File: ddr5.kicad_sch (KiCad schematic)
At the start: 39 parts, among them U1 MT60B2G8HB-48B_A

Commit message: Globlib
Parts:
- C1, C10, C11, C12, C13, C14, C15, C18, C2, C23, C24, C25, C26, C28, C3, C30, C32, C4, C5, C6, C7, C8, C9: footprint ddr5-testbed-footprints:C_0201 -> antmicro-footprints:C_0201; symbol ddr5-testbed:C_100n_0201 -> antmicroCapacitorsmisc:C_100n_0201
- FB1, FB2, FB3: footprint ddr5-testbed-footprints:FB_0805_2012Metric -> antmicro-footprints:FB_0805_2012Metric; symbol ddr5-testbed:FB_220Z_1.5A_0805 -> antmicroFerriteBeadsandChips:FB_220Z_1.5A_WE-CBF_0805
- R1, R5: footprint ddr5-testbed-footprints:R_0402_1005Metric -> antmicro-footprints:R_0402_1005Metric; symbol ddr5-testbed:R_1k_0402 -> antmicroResistors0402:R_1k_0402
- R15, R16, R17, R18, R19, R2, R4, R7: footprint ddr5-testbed-footprints:R_0402_1005Metric -> antmicro-footprints:R_0402_1005Metric; symbol ddr5-testbed:R_0R_0402 -> antmicroResistors0402:R_0R_0402
- R3: footprint ddr5-testbed-footprints:R_0402_1005Metric -> antmicro-footprints:R_0402_1005Metric; symbol ddr5-testbed:R_10k_0402 -> antmicroResistors0402:R_10k_0402
- R6: footprint ddr5-testbed-footprints:R_0402_1005Metric -> antmicro-footprints:R_0402_1005Metric; symbol ddr5-testbed:R_240R_0402 -> antmicroResistors0402:R_240R_0402
- U1: footprint ddr5-testbed-footprints:BGA-82_11x9mm_Layout13x11_P0.8mm_DDR5_MO-210-AN -> antmicro-footprints:BGA-82_11x9mm_Layout13x11_P0.8mm_DDR5_MO-210-AN; symbol ddr5-testbed:MT60B2G8HB-48B_A -> antmicroMemory:MT60B2G8HB-48B_A

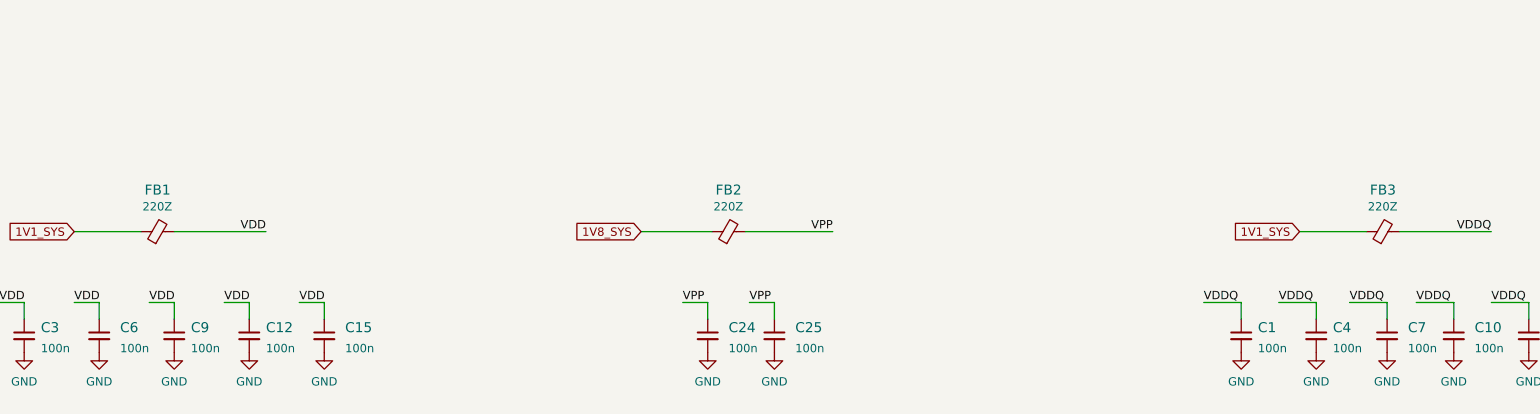
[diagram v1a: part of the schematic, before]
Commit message: Fix broken library references
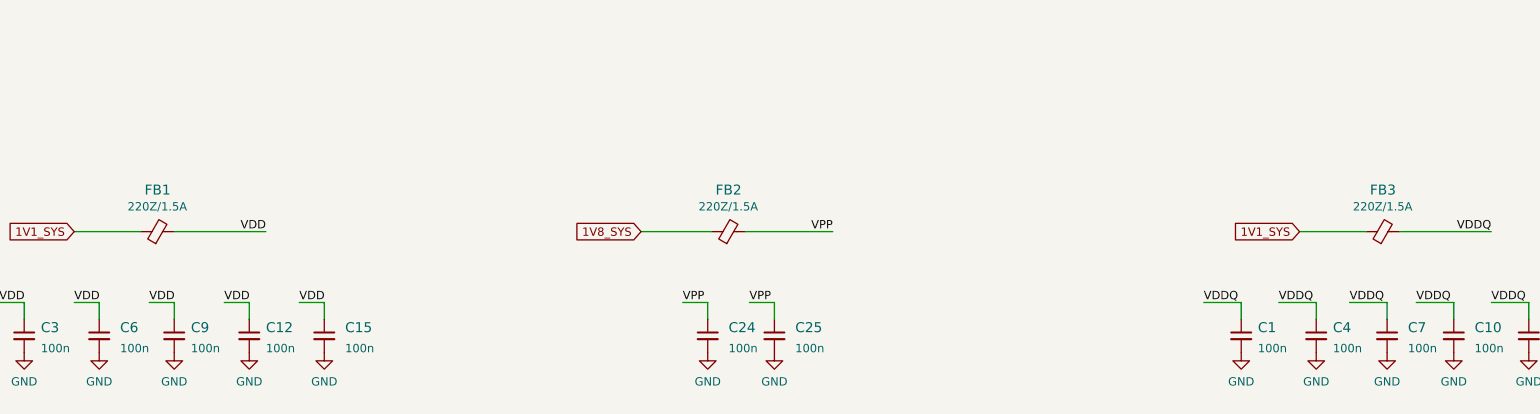
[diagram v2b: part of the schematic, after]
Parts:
- C1, C10, C11, C12, C13, C14, C15, C18, C2, C23, C24, C25, C26, C28, C3, C30, C32, C4, C5, C6, C7, C8, C9: Manufacturer Yaego -> YAGEO; Public (none) -> False
- FB1, FB2, FB3: value FB_220Z_1.5A_0805 -> FB_220Z_1.5A_WE-CBF_0805; Manufacturer Wurth Electronic -> Würth Elektronik; Public (none) -> False; Val 220Z -> 220Z/1.5A
- U1: Manufacturer Micron -> Micron Technology
